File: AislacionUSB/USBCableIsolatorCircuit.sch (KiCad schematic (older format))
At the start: 53 parts, among them CON1 BARREL_JACK, J1 MICRO_USB, J2 IN_VCC, P1 USB_A, U1 PRTR5V0U2X, U2 ADUM5000, U3 7805, U4 PRTR5V0U2X

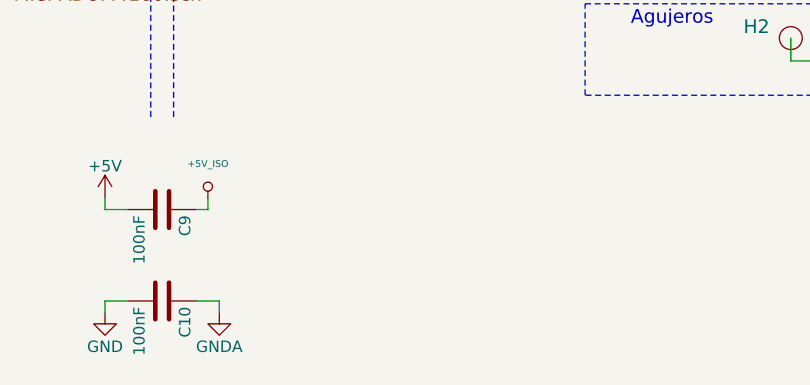
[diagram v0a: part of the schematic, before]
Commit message: Logo en el PCB - Datos del PCB
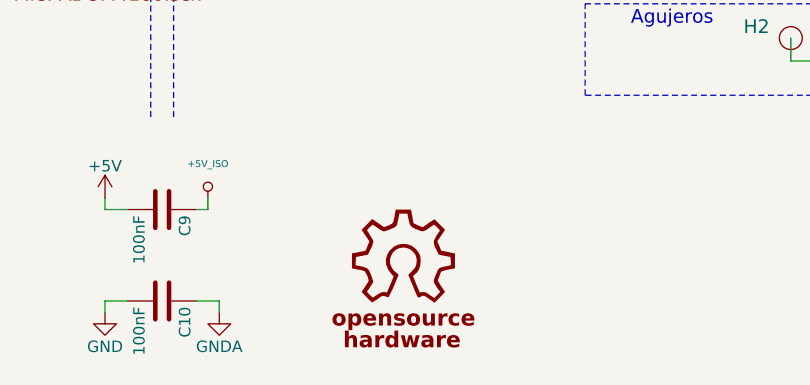
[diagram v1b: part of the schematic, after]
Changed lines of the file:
@@
+	1    0    0    -1
+$EndComp
+$Comp
+L OSHWA #G1
+U 1 1 5796042C
+P 6500 7250
+F 0 "#G1" H 6470 7650 60  0001 C CNN
+F 1 "OSHWA" H 6500 7553 60  0001 C CNN
+F 2 "" H 6500 7250 60  0000 C CNN
+F 3 "" H 6500 7250 60  0000 C CNN
+	1    6500 7250
 	1    0    0    -1
 $EndComp

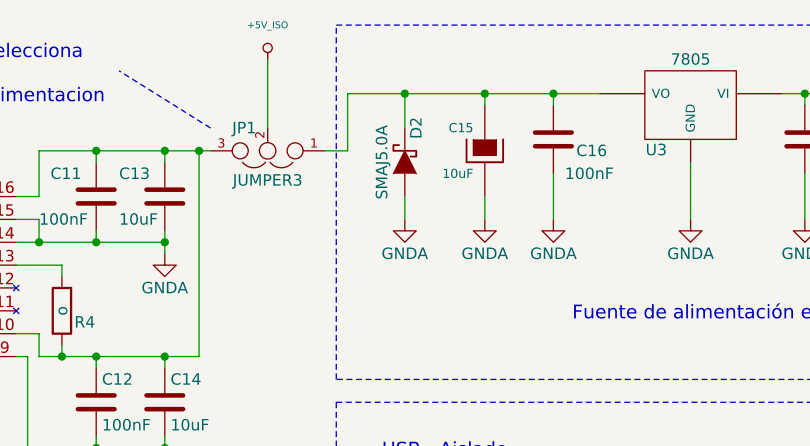
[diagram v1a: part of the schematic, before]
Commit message: Se agregaron los cambios sugueridos en el doc Aislacion USB - Revision PCB  20160725
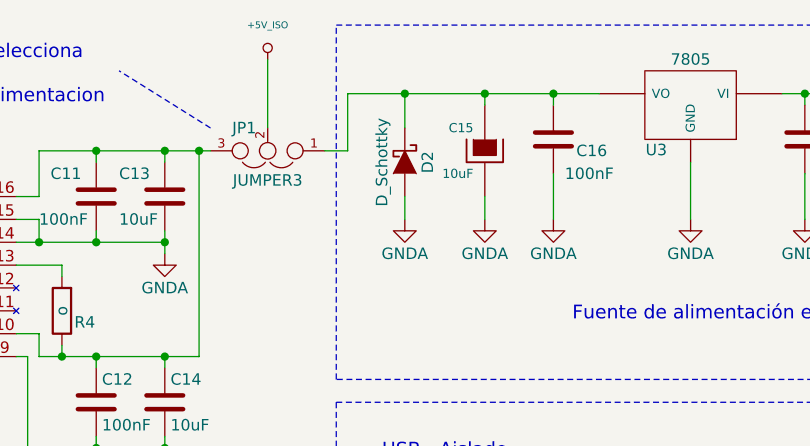
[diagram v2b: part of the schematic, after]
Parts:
- D2: value SMAJ5.0A -> D_Schottky; Desc TVS DIODE 5VWM SMD -> (none); Digikey# SMAJ5.0ABCT-ND -> (none); Manf Bourns -> (none); Manf# SMAJ5.0A -> (none)
- TR1, TR2: footprint AislacionUSB:SRF2012 -> AislacionUSB:SRF2012-HandSoldering
- U1, U4: footprint AislacionUSB:SOT-143-4 -> AislacionUSB:SOT-143-4-HandSoldering
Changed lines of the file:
@@
-$EndComp
-$Comp
-L D_Schottky D2
-U 1 1 577C52B5
-P 7600 1150
-F 0 "D2" H 7450 1100 50  0000 C CNN
-F 1 "SMAJ5.0A" H 7600 1250 50  0000 C CNN
-F 2 "AislacionUSB:DO-214AC_SMA" H 7600 1150 50  0001 C CNN
-F 3 "" H 7600 1150 50  0000 C CNN
-F 4 "SMAJ5.0ABCT-ND" H 7600 1150 60  0001 C CNN "Digikey#"
-F 5 "SMAJ5.0A" H 7600 1150 60  0001 C CNN "Manf#"
-F 6 "Bourns" H 7600 1150 60  0001 C CNN "Manf"
-F 7 "TVS DIODE 5VWM SMD" H 7600 1150 60  0001 C CNN "Desc"
-	1    7600 1150
-	0    -1   1    0
 $EndComp
 $Comp
@@
 F 0 "TR1" H 3150 5750 60  0000 C CNN
 F 1 "SRF2012" V 2850 5550 60  0000 C CNN
-F 2 "AislacionUSB:SRF2012" H 3150 5550 60  0001 C CNN
+F 2 "AislacionUSB:SRF2012-HandSoldering" H 3150 5550 60  0001 C CNN
 F 3 "~" H 3150 5550 60  0000 C CNN
 F 4 "SRF2012-900YCT-ND" H 3150 5550 60  0001 C CNN "Digikey#"
@@
 F 0 "U1" H 2250 6600 70  0000 C CNN
 F 1 "PRTR5V0U2X" H 2250 5950 70  0000 C CNN
-F 2 "AislacionUSB:SOT-143-4" H 3800 5650 60  0001 C CNN
+F 2 "AislacionUSB:SOT-143-4-HandSoldering" H 3800 5650 60  0001 C CNN
 F 3 "~" H 3800 5650 60  0000 C CNN
 F 4 "CM1213A-02SROSCT-ND" H 2250 6300 60  0001 C CNN "Digikey#"
@@
 F 0 "U4" H 9450 4600 70  0000 C CNN
 F 1 "PRTR5V0U2X" H 9450 3950 70  0000 C CNN
-F 2 "AislacionUSB:SOT-143-4" H 11000 3650 60  0001 C CNN
+F 2 "AislacionUSB:SOT-143-4-HandSoldering" H 11000 3650 60  0001 C CNN
 F 3 "~" H 11000 3650 60  0000 C CNN
 F 4 "CM1213A-02SROSCT-ND" H 9450 4300 60  0001 C CNN "Digikey#"
@@
 F 0 "TR2" H 8400 3850 60  0000 C CNN
 F 1 "SRF2012" V 8100 3650 60  0000 C CNN
-F 2 "AislacionUSB:SRF2012" H 8400 3650 60  0001 C CNN
+F 2 "AislacionUSB:SRF2012-HandSoldering" H 8400 3650 60  0001 C CNN
 F 3 "~" H 8400 3650 60  0000 C CNN
 F 4 "SRF2012-900YCT-ND" H 8400 3650 60  0001 C CNN "Digikey#"
@@
 	1    0    0    -1
 $EndComp
+$Comp
+L D_Schottky D2
+U 1 1 579656C1
+P 7600 1150
+F 0 "D2" H 7600 1250 50  0000 C CNN
+F 1 "D_Schottky" H 7600 1050 50  0000 C CNN
+F 2 "AislacionUSB:DO-214AC_SMA" H 7600 1150 50  0001 C CNN
+F 3 "" H 7600 1150 50  0000 C CNN
+	1    7600 1150
+	0    1    1    0
+$EndComp
 $EndSCHEMATC

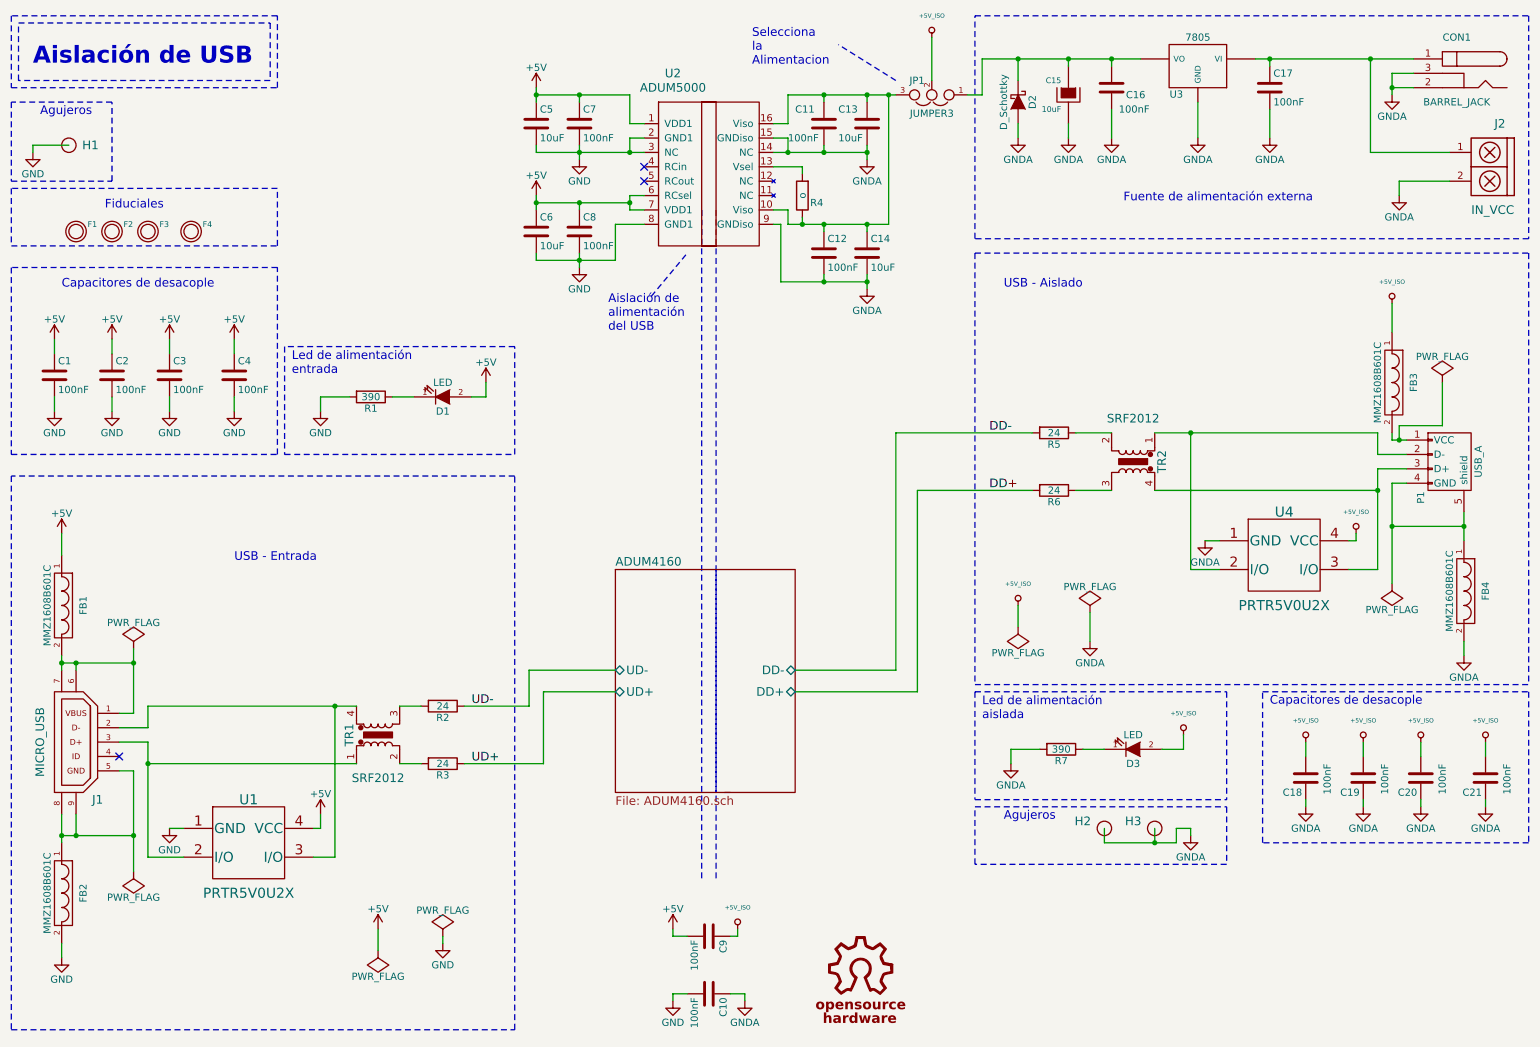
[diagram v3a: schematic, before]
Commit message: Se desconectaron los agujeros del GND
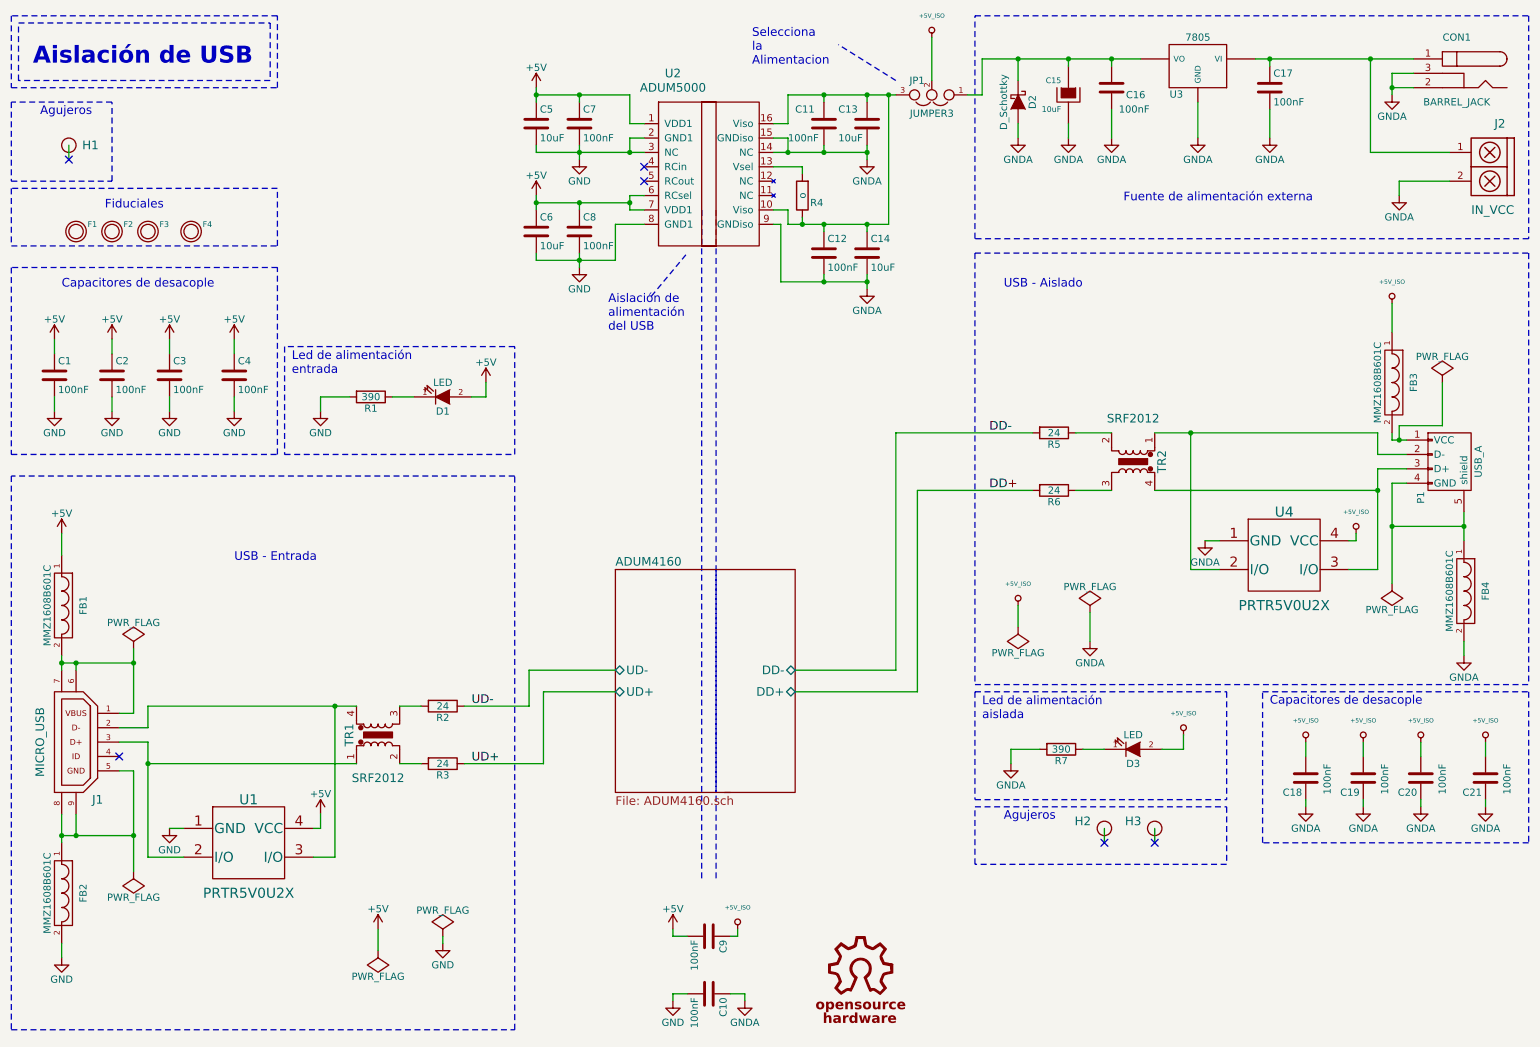
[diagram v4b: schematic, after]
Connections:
- net GND: no longer H1.1
- net GNDA: no longer H2.1, H3.1
- no-connect marks 3 -> 6
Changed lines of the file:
@@
-$EndComp
-$Comp
-L GNDA #PWR025
-U 1 1 57861B0A
-P 8800 6250
-F 0 "#PWR025" H 8800 6000 50  0001 C CNN
-F 1 "GNDA" H 8800 6100 50  0000 C CNN
-F 2 "" H 8800 6250 50  0000 C CNN
-F 3 "" H 8800 6250 50  0000 C CNN
-	1    8800 6250
-	1    0    0    -1
 $EndComp
 $Comp
@@
 $EndComp
 $Comp
-L +5V #PWR026
+L +5V #PWR025
 U 1 1 578640A5
 P 3900 3100
-F 0 "#PWR026" H 3900 2950 50  0001 C CNN
+F 0 "#PWR025" H 3900 2950 50  0001 C CNN
 F 1 "+5V" H 3900 3240 50  0000 C CNN
 F 2 "" H 3900 3100 50  0000 C CNN
@@
 $EndComp
 $Comp
-L GND #PWR027
+L GND #PWR026
 U 1 1 578645CC
 P 2750 3300
-F 0 "#PWR027" H 2750 3050 50  0001 C CNN
+F 0 "#PWR026" H 2750 3050 50  0001 C CNN
 F 1 "GND" H 2750 3150 50  0000 C CNN
 F 2 "" H 2750 3300 50  0000 C CNN
@@
 $EndComp
 $Comp
-L GND #PWR028
+L GND #PWR027
 U 1 1 57867AFA
 P 4550 2300
-F 0 "#PWR028" H 4550 2050 50  0001 C CNN
+F 0 "#PWR027" H 4550 2050 50  0001 C CNN
 F 1 "GND" H 4550 2150 50  0000 C CNN
 F 2 "" H 4550 2300 50  0000 C CNN
@@
 $EndComp
 $Comp
-L GND #PWR029
+L GND #PWR028
 U 1 1 57869BFF
 P 4550 1550
-F 0 "#PWR029" H 4550 1300 50  0001 C CNN
+F 0 "#PWR028" H 4550 1300 50  0001 C CNN
 F 1 "GND" H 4550 1400 50  0000 C CNN
 F 2 "" H 4550 1550 50  0000 C CNN
@@
 $EndComp
 $Comp
-L +5V #PWR030
+L +5V #PWR029
 U 1 1 57869C97
 P 4250 1050
-F 0 "#PWR030" H 4250 900 50  0001 C CNN
+F 0 "#PWR029" H 4250 900 50  0001 C CNN
 F 1 "+5V" H 4250 1190 50  0000 C CNN
 F 2 "" H 4250 1050 50  0000 C CNN
@@
 $EndComp
 $Comp
-L +5V #PWR031
+L +5V #PWR030
 U 1 1 57869D2F
 P 4250 1800
-F 0 "#PWR031" H 4250 1650 50  0001 C CNN
+F 0 "#PWR030" H 4250 1650 50  0001 C CNN
 F 1 "+5V" H 4250 1940 50  0000 C CNN
 F 2 "" H 4250 1800 50  0000 C CNN
@@
 $EndComp
 $Comp
-L GNDA #PWR032
+L GNDA #PWR031
 U 1 1 5786D343
 P 6550 1550
-F 0 "#PWR032" H 6550 1300 50  0001 C CNN
+F 0 "#PWR031" H 6550 1300 50  0001 C CNN
 F 1 "GNDA" H 6550 1400 50  0000 C CNN
 F 2 "" H 6550 1550 50  0000 C CNN
@@
 $EndComp
 $Comp
-L GNDA #PWR033
+L GNDA #PWR032
 U 1 1 5786D41A
 P 6550 2450
-F 0 "#PWR033" H 6550 2200 50  0001 C CNN
+F 0 "#PWR032" H 6550 2200 50  0001 C CNN
 F 1 "GNDA" H 6550 2300 50  0000 C CNN
 F 2 "" H 6550 2450 50  0000 C CNN
@@
 $EndComp
 $Comp
-L +5V_ISO #PWR034
+L +5V_ISO #PWR033
 U 1 1 57857B44
 P 7000 700
-F 0 "#PWR034" H 7000 790 20  0001 C CNN
+F 0 "#PWR033" H 7000 790 20  0001 C CNN
 F 1 "+5V_ISO" H 7000 850 30  0000 C CNN
 F 2 "" H 7000 700 60  0000 C CNN
@@
 DD+
 $Comp
-L +5V_ISO #PWR035
+L +5V_ISO #PWR034
 U 1 1 5785C5F6
 P 9600 5600
-F 0 "#PWR035" H 9600 5690 20  0001 C CNN
+F 0 "#PWR034" H 9600 5690 20  0001 C CNN
 F 1 "+5V_ISO" H 9600 5750 30  0000 C CNN
 F 2 "" H 9600 5600 60  0000 C CNN
@@
 $EndComp
 $Comp
-L +5V_ISO #PWR036
+L +5V_ISO #PWR035
 U 1 1 5785CE92
 P 10000 5600
-F 0 "#PWR036" H 10000 5690 20  0001 C CNN
+F 0 "#PWR035" H 10000 5690 20  0001 C CNN
 F 1 "+5V_ISO" H 10000 5750 30  0000 C CNN
 F 2 "" H 10000 5600 60  0000 C CNN
@@
 $EndComp
 $Comp
-L +5V_ISO #PWR037
+L +5V_ISO #PWR036
 U 1 1 5785CF9C
 P 10400 5600
-F 0 "#PWR037" H 10400 5690 20  0001 C CNN
+F 0 "#PWR036" H 10400 5690 20  0001 C CNN
 F 1 "+5V_ISO" H 10400 5750 30  0000 C CNN
 F 2 "" H 10400 5600 60  0000 C CNN
@@
 $EndComp
 $Comp
-L +5V_ISO #PWR038
+L +5V_ISO #PWR037
 U 1 1 5785D0E3
 P 10850 5600
-F 0 "#PWR038" H 10850 5690 20  0001 C CNN
+F 0 "#PWR037" H 10850 5690 20  0001 C CNN
 F 1 "+5V_ISO" H 10850 5750 30  0000 C CNN
 F 2 "" H 10850 5600 60  0000 C CNN
@@
 $EndComp
 $Comp
-L +5V_ISO #PWR039
+L +5V_ISO #PWR038
 U 1 1 5785D97F
 P 10200 2550
-F 0 "#PWR039" H 10200 2640 20  0001 C CNN
+F 0 "#PWR038" H 10200 2640 20  0001 C CNN
 F 1 "+5V_ISO" H 10200 2700 30  0000 C CNN
 F 2 "" H 10200 2550 60  0000 C CNN
@@
 $EndComp
 $Comp
-L +5V_ISO #PWR040
+L +5V_ISO #PWR039
 U 1 1 5785ED54
 P 9950 4150
-F 0 "#PWR040" H 9950 4240 20  0001 C CNN
+F 0 "#PWR039" H 9950 4240 20  0001 C CNN
 F 1 "+5V_ISO" H 9950 4300 30  0000 C CNN
 F 2 "" H 9950 4150 60  0000 C CNN
@@
 $EndComp
 $Comp
-L +5V_ISO #PWR041
+L +5V_ISO #PWR040
 U 1 1 5786351C
 P 8750 5550
-F 0 "#PWR041" H 8750 5640 20  0001 C CNN
+F 0 "#PWR040" H 8750 5640 20  0001 C CNN
 F 1 "+5V_ISO" H 8750 5700 30  0000 C CNN
 F 2 "" H 8750 5550 60  0000 C CNN
@@
 $EndComp
 $Comp
-L +5V_ISO #PWR042
+L +5V_ISO #PWR041
 U 1 1 5786C056
 P 5650 6900
-F 0 "#PWR042" H 5650 6990 20  0001 C CNN
+F 0 "#PWR041" H 5650 6990 20  0001 C CNN
 F 1 "+5V_ISO" H 5650 7050 30  0000 C CNN
 F 2 "" H 5650 6900 60  0000 C CNN
@@
 $EndComp
 $Comp
-L GNDA #PWR043
+L GNDA #PWR042
 U 1 1 5786C0FA
 P 5700 7400
-F 0 "#PWR043" H 5700 7150 50  0001 C CNN
+F 0 "#PWR042" H 5700 7150 50  0001 C CNN
 F 1 "GNDA" H 5700 7250 50  0000 C CNN
 F 2 "" H 5700 7400 50  0000 C CNN
@@
 $EndComp
 $Comp
-L GND #PWR044
+L GND #PWR043
 U 1 1 5786C468
 P 5200 7400
-F 0 "#PWR044" H 5200 7150 50  0001 C CNN
+F 0 "#PWR043" H 5200 7150 50  0001 C CNN
 F 1 "GND" H 5200 7250 50  0000 C CNN
 F 2 "" H 5200 7400 50  0000 C CNN
@@
 $EndComp
 $Comp
-L +5V #PWR045
+L +5V #PWR044
 U 1 1 5786CF39
 P 5200 6900
-F 0 "#PWR045" H 5200 6750 50  0001 C CNN
+F 0 "#PWR044" H 5200 6750 50  0001 C CNN
 F 1 "+5V" H 5200 7040 50  0000 C CNN
 F 2 "" H 5200 6900 50  0000 C CNN
@@
 NoConn ~ 1350 5700
 $Comp
-L PWR_FLAG #FLG046
+L PWR_FLAG #FLG045
 U 1 1 57901FA7
 P 1450 4950
-F 0 "#FLG046" H 1450 5045 50  0001 C CNN
+F 0 "#FLG045" H 1450 5045 50  0001 C CNN
 F 1 "PWR_FLAG" H 1450 5130 50  0000 C CNN
 F 2 "" H 1450 4950 50  0000 C CNN
@@
 $EndComp
 $Comp
-L PWR_FLAG #FLG047
+L PWR_FLAG #FLG046
 U 1 1 57902051
 P 1450 6500
-F 0 "#FLG047" H 1450 6595 50  0001 C CNN
+F 0 "#FLG046" H 1450 6595 50  0001 C CNN
 F 1 "PWR_FLAG" H 1450 6680 50  0000 C CNN
 F 2 "" H 1450 6500 50  0000 C CNN
@@
 Connection ~ 1450 6250
 $Comp
-L PWR_FLAG #FLG048
+L PWR_FLAG #FLG047
 U 1 1 579025E4
 P 10200 4500
-F 0 "#FLG048" H 10200 4595 50  0001 C CNN
+F 0 "#FLG047" H 10200 4595 50  0001 C CNN
 F 1 "PWR_FLAG" H 10200 4680 50  0000 C CNN
 F 2 "" H 10200 4500 50  0000 C CNN
@@
 Connection ~ 10200 4100
 $Comp
-L PWR_FLAG #FLG049
+L PWR_FLAG #FLG048
 U 1 1 5790310F
 P 10550 3100
-F 0 "#FLG049" H 10550 3195 50  0001 C CNN
+F 0 "#FLG048" H 10550 3195 50  0001 C CNN
 F 1 "PWR_FLAG" H 10550 3280 50  0000 C CNN
 F 2 "" H 10550 3100 50  0000 C CNN
@@
 Connection ~ 10250 3500
 $Comp
-L PWR_FLAG #FLG050
+L PWR_FLAG #FLG049
 U 1 1 57904563
 P 3600 6950
-F 0 "#FLG050" H 3600 7045 50  0001 C CNN
+F 0 "#FLG049" H 3600 7045 50  0001 C CNN
 F 1 "PWR_FLAG" H 3600 7130 50  0000 C CNN
 F 2 "" H 3600 6950 50  0000 C CNN
@@
 $EndSheet
 $Comp
-L PWR_FLAG #FLG051
+L PWR_FLAG #FLG050
 U 1 1 57907C7B
 P 7600 4800
-F 0 "#FLG051" H 7600 4895 50  0001 C CNN
+F 0 "#FLG050" H 7600 4895 50  0001 C CNN
 F 1 "PWR_FLAG" H 7600 4980 50  0000 C CNN
 F 2 "" H 7600 4800 50  0000 C CNN
@@
 	950  4150 950  4300
 $Comp
-L GND #PWR052
+L GND #PWR051
 U 1 1 5790C008
 P 3600 7000
-F 0 "#PWR052" H 3600 6750 50  0001 C CNN
+F 0 "#PWR051" H 3600 6750 50  0001 C CNN
 F 1 "GND" H 3600 6850 50  0000 C CNN
 F 2 "" H 3600 7000 50  0000 C CNN
@@
 Connection ~ 1450 5050
 $Comp
-L GNDA #PWR053
+L GNDA #PWR052
 U 1 1 5785B144
 P 10700 5000
-F 0 "#PWR053" H 10700 4750 50  0001 C CNN
+F 0 "#PWR052" H 10700 4750 50  0001 C CNN
 F 1 "GNDA" H 10700 4850 50  0000 C CNN
 F 2 "" H 10700 5000 50  0000 C CNN
@@
 $EndComp
 $Comp
-L GNDA #PWR054
+L GNDA #PWR053
 U 1 1 5790D610
 P 8100 4900
-F 0 "#PWR054" H 8100 4650 50  0001 C CNN
+F 0 "#PWR053" H 8100 4650 50  0001 C CNN
 F 1 "GNDA" H 8100 4750 50  0000 C CNN
 F 2 "" H 8100 4900 50  0000 C CNN
@@
 $EndComp
 $Comp
-L PWR_FLAG #FLG055
+L PWR_FLAG #FLG054
 U 1 1 5790D6D2
 P 8100 4700
-F 0 "#FLG055" H 8100 4795 50  0001 C CNN
+F 0 "#FLG054" H 8100 4795 50  0001 C CNN
 F 1 "PWR_FLAG" H 8100 4880 50  0000 C CNN
 F 2 "" H 8100 4700 50  0000 C CNN
@@
 $EndComp
 $Comp
-L +5V_ISO #PWR056
+L +5V_ISO #PWR055
 U 1 1 5794D9D2
 P 7600 4650
-F 0 "#PWR056" H 7600 4740 20  0001 C CNN
+F 0 "#PWR055" H 7600 4740 20  0001 C CNN
 F 1 "+5V_ISO" H 7600 4800 30  0000 C CNN
 F 2 "" H 7600 4650 60  0000 C CNN
@@
 	7600 4650 7600 4800
 $Comp
-L PWR_FLAG #FLG057
+L PWR_FLAG #FLG056
 U 1 1 5794E482
 P 3150 7050
-F 0 "#FLG057" H 3150 7145 50  0001 C CNN
+F 0 "#FLG056" H 3150 7145 50  0001 C CNN
 F 1 "PWR_FLAG" H 3150 7230 50  0000 C CNN
 F 2 "" H 3150 7050 50  0000 C CNN
@@
 	3150 6900 3150 7050
 $Comp
-L +5V #PWR058
+L +5V #PWR057
 U 1 1 5794E4FF
 P 3150 6900
-F 0 "#PWR058" H 3150 6750 50  0001 C CNN
+F 0 "#PWR057" H 3150 6750 50  0001 C CNN
 F 1 "+5V" H 3150 7040 50  0000 C CNN
 F 2 "" H 3150 6900 50  0000 C CNN
@@
 	7300 6450 7300 6050
 $Comp
-L GND #PWR059
-U 1 1 57958BB6
-P 750 1500
-F 0 "#PWR059" H 750 1250 50  0001 C CNN
-F 1 "GND" H 750 1350 50  0000 C CNN
-F 2 "" H 750 1500 50  0000 C CNN
-F 3 "" H 750 1500 50  0000 C CNN
-	1    750  1500
-	1    0    0    -1
-$EndComp
-Wire Wire Line
-	750  1500 750  1450
-Wire Wire Line
-	750  1450 1000 1450
-Wire Wire Line
-	8200 6200 8200 6300
-Wire Wire Line
-	8200 6300 8700 6300
-Wire Wire Line
-	8550 6300 8550 6200
-Wire Wire Line
-	8700 6300 8700 6200
-Wire Wire Line
-	8700 6200 8800 6200
-Wire Wire Line
-	8800 6200 8800 6250
-Connection ~ 8550 6300
-$Comp
-L GNDA #PWR060
+L GNDA #PWR059
 U 1 1 5795C939
 P 9600 6050
-F 0 "#PWR060" H 9600 5800 50  0001 C CNN
+F 0 "#PWR059" H 9600 5800 50  0001 C CNN
 F 1 "GNDA" H 9600 5900 50  0000 C CNN
 F 2 "" H 9600 6050 50  0000 C CNN
@@
 	0    1    1    0
 $EndComp
+NoConn ~ 8550 6300
+NoConn ~ 8200 6300
+Wire Wire Line
+	8200 6200 8200 6300
+Wire Wire Line
+	8550 6200 8550 6300
+Wire Wire Line
+	1000 1450 1000 1550
+NoConn ~ 1000 1550
 $EndSCHEMATC
